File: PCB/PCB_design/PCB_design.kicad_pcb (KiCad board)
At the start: 2 copper layers, 83.5 x 68.2 mm, 49 parts, among them J2 Conn_01x03_Pin, J3 Conn_01x01_Pin, J4 Conn_01x01_Pin, J5 Conn_01x01_Pin, J6 Conn_01x01_Pin, J7 Conn_02x04_Counter_Clockwise, K1 Relay_SPST-NO, K2 Relay_SPST-NO, K3 Relay_SPST-NO, K4 Relay_SPST-NO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

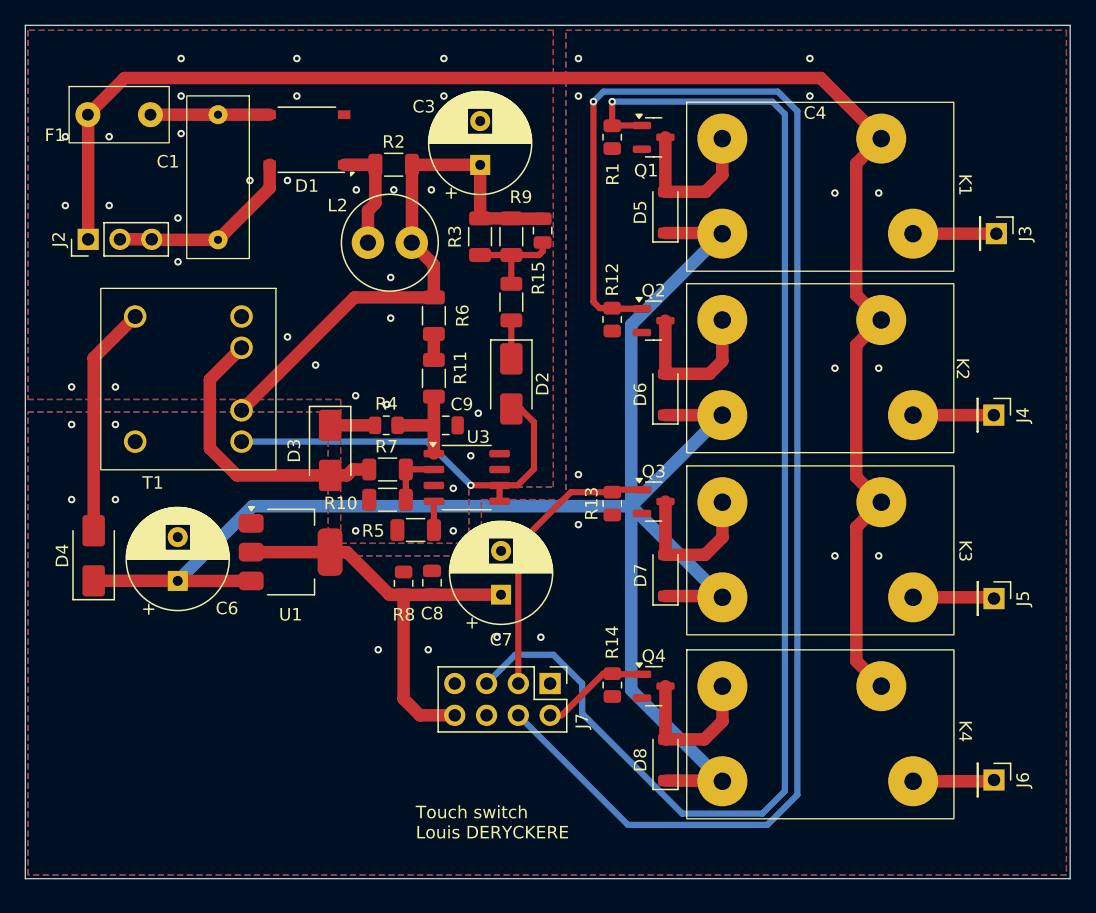
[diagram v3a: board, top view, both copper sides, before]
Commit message: Routage compact & génération gerber
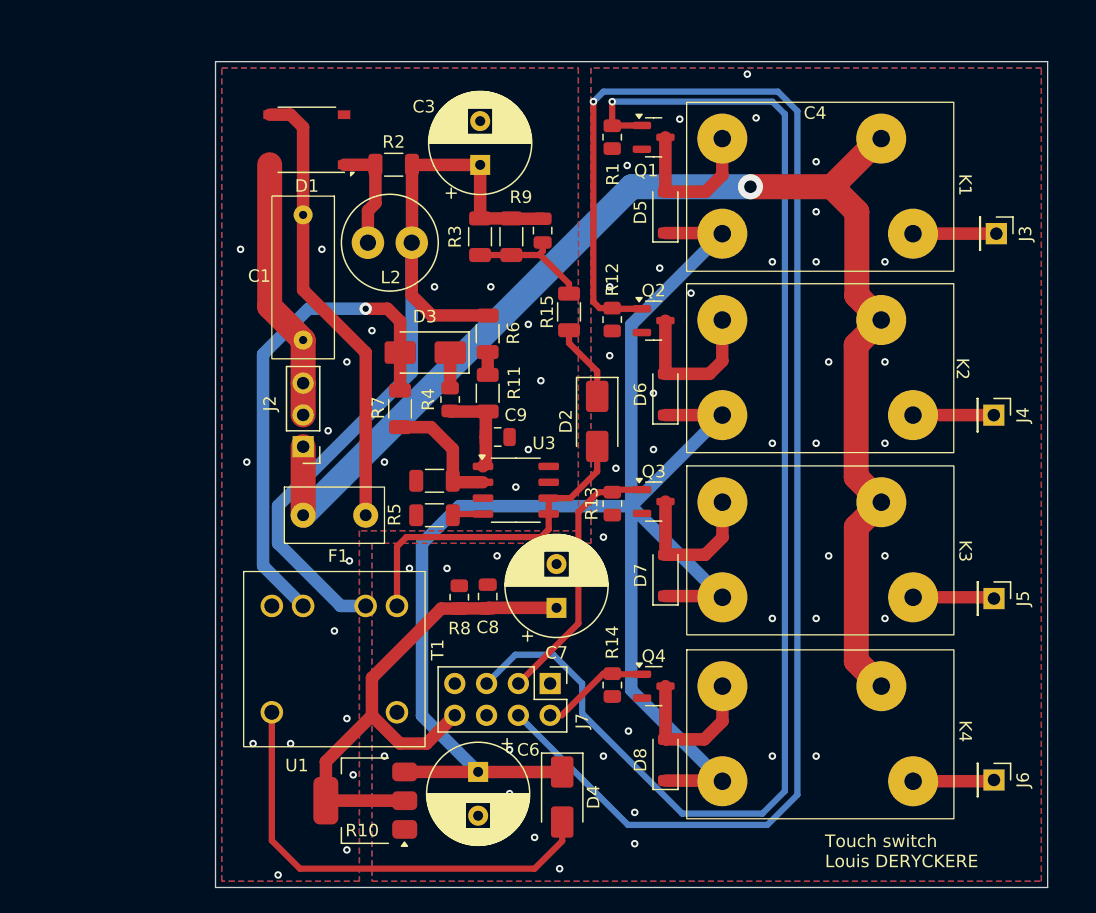
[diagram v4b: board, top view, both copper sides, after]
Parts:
- moved D4 42.1 mm to (121.2, 86.8), turned to -90 degrees
- moved F1 36.3 mm to (103.0, 64.2)
- moved T1 33.5 mm to (98.0, 80.0), turned to 0 degrees
- moved C6 28.4 mm to (114.5, 84.8), turned to -90 degrees
- moved J2 23.9 mm to (100.5, 58.8), turned to 180 degrees
- moved U1 20.7 mm to (105.5, 87.1), turned to 180 degrees
- moved D3 10.9 mm to (110.2, 51.2), turned to 180 degrees
- moved C1 10.5 mm to (100.5, 40.2)
- moved D2 7.49 mm to (124.0, 56.8)
- moved R4 5.50 mm to (112.2, 55.0), turned to 90 degrees
- moved R7 4.95 mm to (108.2, 55.8), turned to -90 degrees
- moved R15 4.68 mm to (121.8, 48.0)
- moved C8 4.58 mm to (115.2, 70.8)
- moved R8 4.58 mm to (113.0, 70.8)
- moved C7 4.55 mm to (120.8, 71.7)
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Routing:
- net Net-(C1-Pad1): track 9.53 -> 36.2 mm
- net +310VDC: track 45.2 -> 69.5 mm
- net Net-(D4-A): track 18.5 -> 36.8 mm
- net Vaux: track 22.9 -> 39.8 mm, vias 0 -> 1
- net L: track 125.3 -> 109.0 mm, vias 0 -> 1
- net +3.3V: track 34.3 -> 43.2 mm
- net C: track 32.6 -> 26.7 mm, vias 1 -> 0
- net N: track 15.6 -> 21.1 mm
- net Net-(U3-FB): track 4.66 -> 9.94 mm
- net Net-(D2-K): track 3.08 -> 6.22 mm
- net Net-(C4-Pad2): track 8.13 -> 9.97 mm
- net CT3: track 22.8 -> 21.5 mm
- net Net-(D3-K): track 3.58 -> 2.84 mm
- net +5VDC: track 140.6 -> 140.0 mm
- net GND2: vias 20 -> 41
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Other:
- board size 83.5 x 68.2 mm -> 66.5 x 66 mm

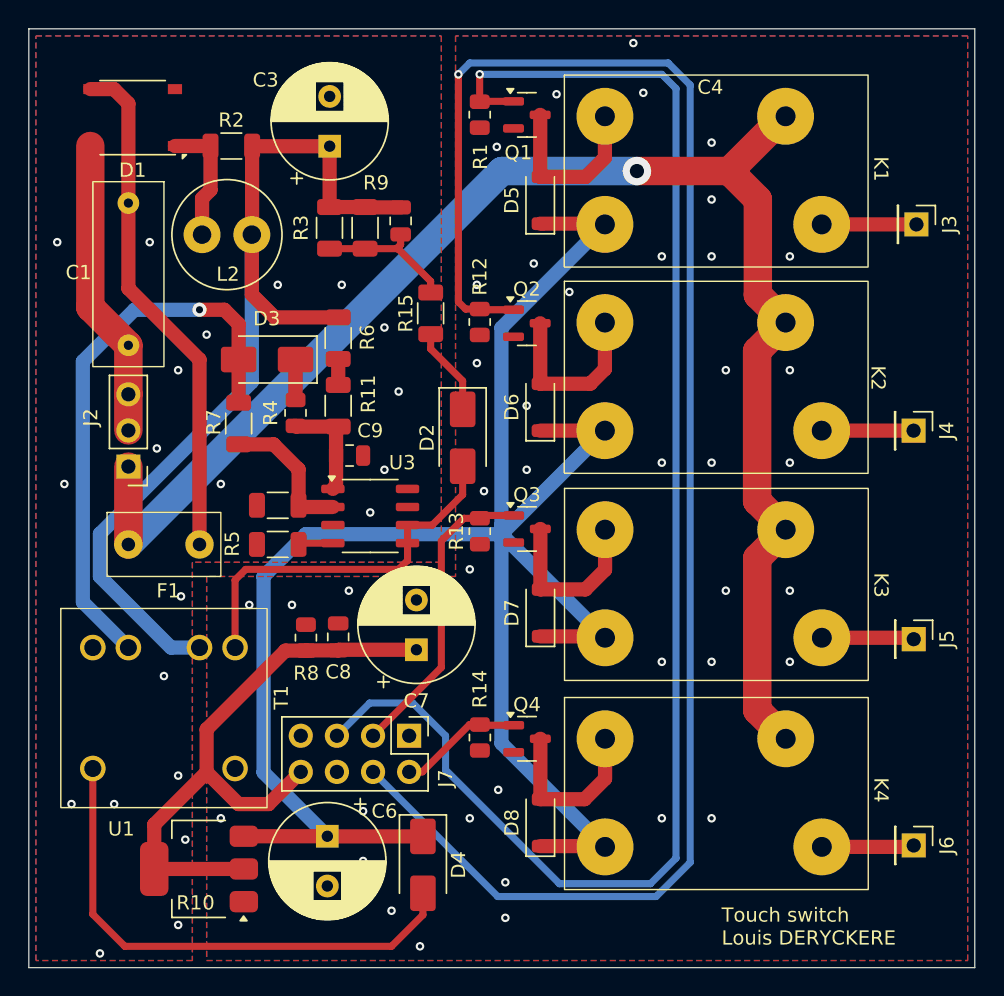
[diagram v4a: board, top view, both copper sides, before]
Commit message: Correction footprint relais
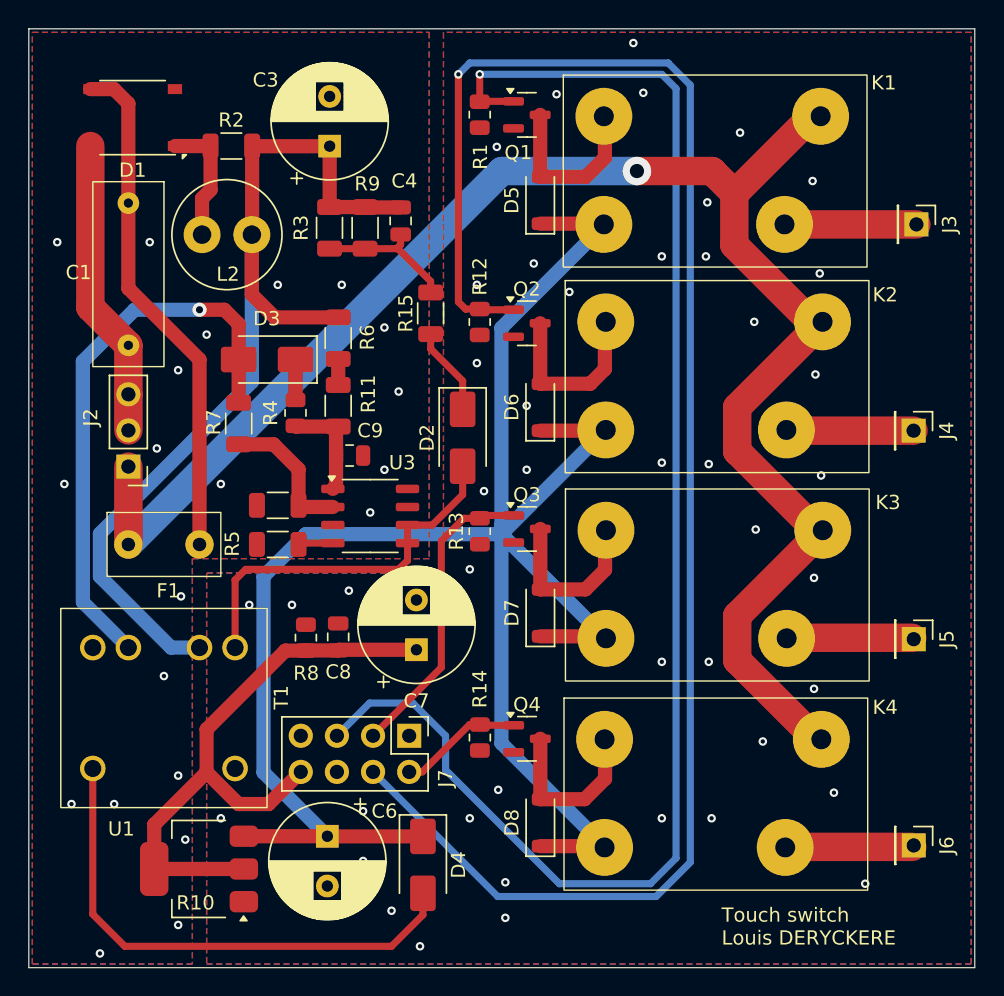
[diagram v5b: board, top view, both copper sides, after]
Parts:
- moved K2 0.08 mm to (134.1, 56.2)
- moved K3 0.08 mm to (134.1, 70.8)
- moved K1 0.07 mm to (133.9, 41.8)
- moved K4 0.05 mm to (134.0, 85.5)
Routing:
- net L: track 109.0 -> 120.1 mm
- net Net-(J3-Pin_1): track 6.66 -> 9.28 mm
- net Net-(J6-Pin_1): track 6.50 -> 9.09 mm
- net Net-(J4-Pin_1): track 6.46 -> 8.96 mm
- net Net-(J5-Pin_1): track 6.50 -> 8.99 mm
- net GND2: vias 41 -> 45

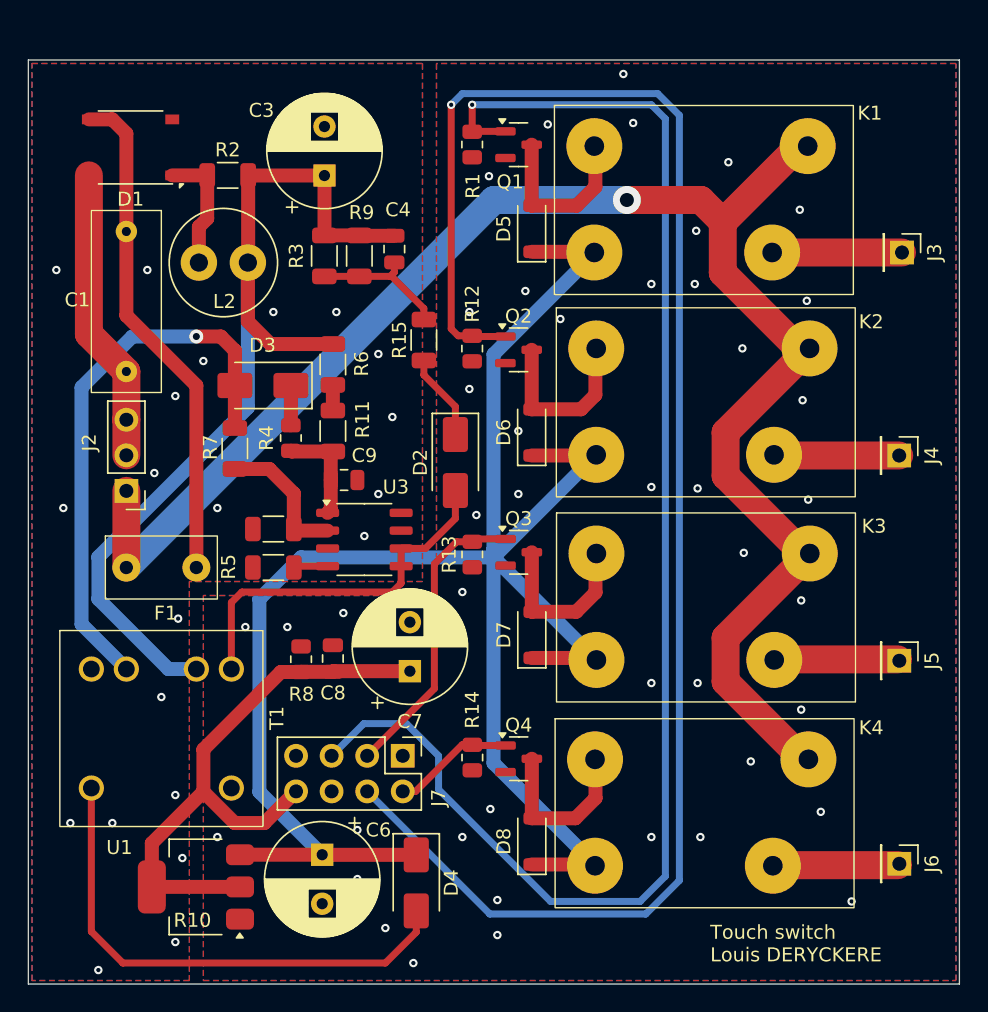
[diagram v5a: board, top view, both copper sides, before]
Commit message: Correction footprints relais et transfo
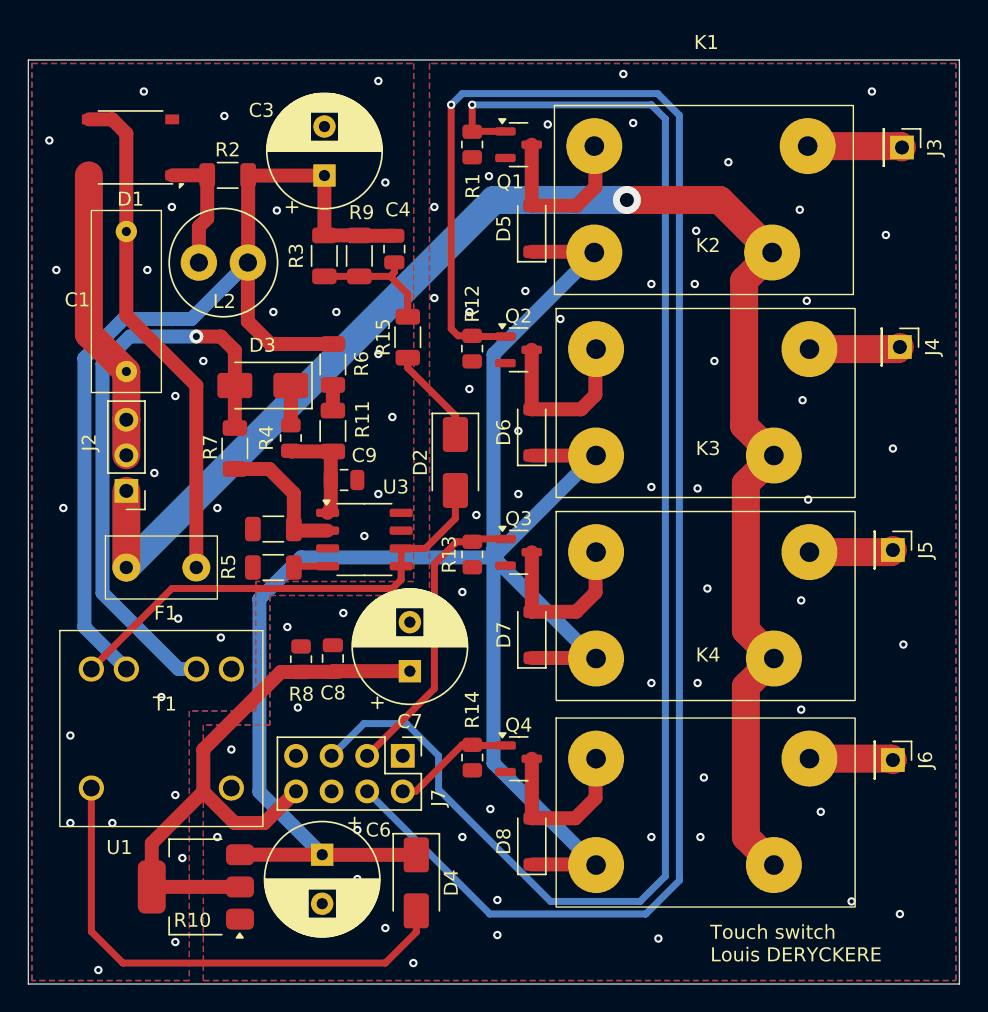
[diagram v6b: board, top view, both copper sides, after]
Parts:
- T1: footprint Touch_Switch_Custom:Transformer_V2 -> Touch_Switch_Custom:Transformer_V2_1
- moved J5 7.92 mm to (155.2, 63.0)
- moved J4 7.75 mm to (155.8, 48.5)
- moved J3 7.50 mm to (155.9, 34.2)
- moved J6 7.42 mm to (155.2, 78.0)
- moved R15 1.17 mm to (120.6, 47.8)
- moved K3 0.10 mm to (134.1, 70.8)
- moved K4 0.09 mm to (134.1, 85.5)
- moved K2 0.05 mm to (134.1, 56.2)
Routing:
- net L: track 120.1 -> 113.0 mm
- net C: track 26.7 -> 33.8 mm
- net Net-(J6-Pin_1): track 9.09 -> 6.00 mm
- net Net-(J5-Pin_1): track 8.99 -> 6.02 mm
- net Net-(J4-Pin_1): track 8.96 -> 6.52 mm
- net Net-(J3-Pin_1): track 9.28 -> 7.19 mm
- net Vaux: track 39.8 -> 41.5 mm
- net Net-(C4-Pad2): track 9.97 -> 9.23 mm
- net Net-(D2-K): track 6.22 -> 6.90 mm
- net GND2: vias 45 -> 54
- net GND: vias 21 -> 30

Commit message: Ajout mounting holes
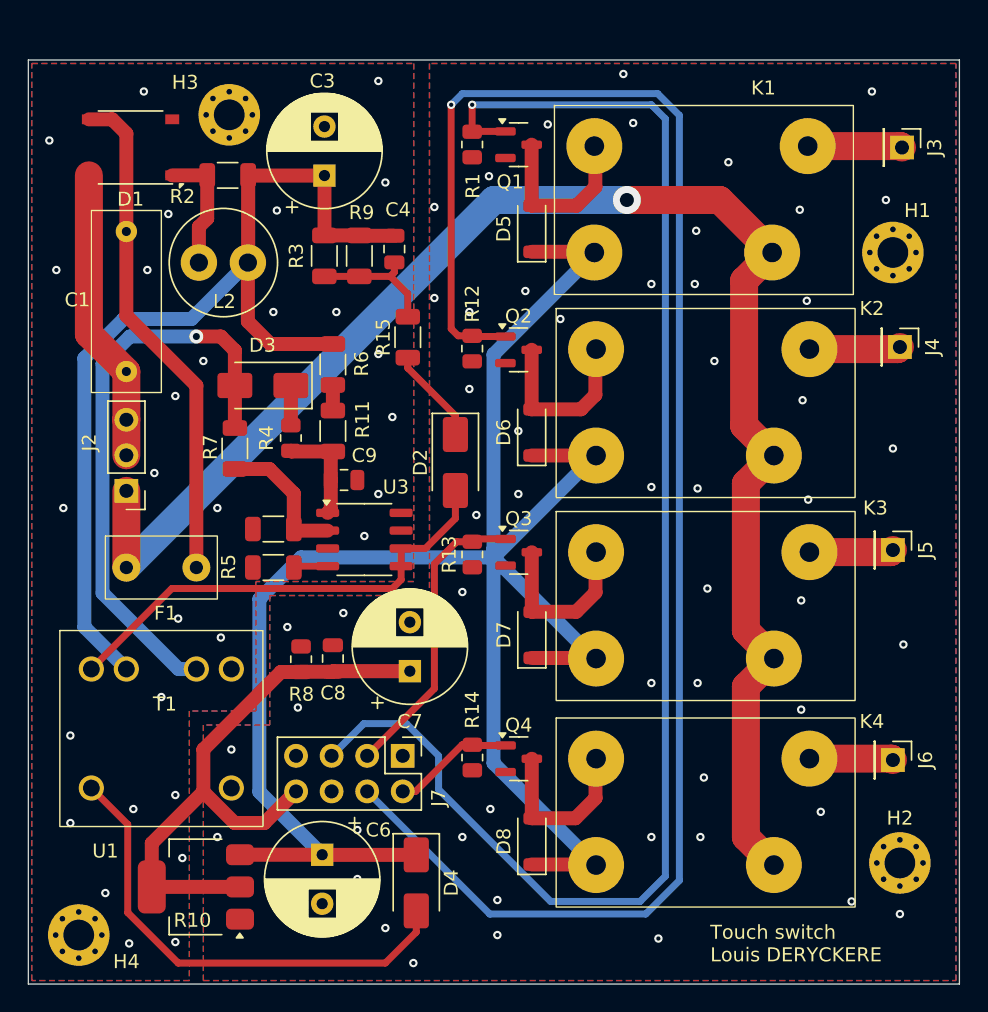
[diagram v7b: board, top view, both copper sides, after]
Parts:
- added H1: MountingHole, MountingHole:MountingHole_2.2mm_M2_Pad_Via, F.Cu at (155.2, 41.8)
- added H2: MountingHole, MountingHole:MountingHole_2.2mm_M2_Pad_Via, F.Cu at (155.8, 85.3)
- added H3: MountingHole, MountingHole:MountingHole_2.2mm_M2_Pad_Via, F.Cu at (107.8, 31.9)
- added H4: MountingHole, MountingHole:MountingHole_2.2mm_M2_Pad_Via, F.Cu at (97.1, 90.5)
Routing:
- net Net-(D4-A): track 36.8 -> 34.5 mm
